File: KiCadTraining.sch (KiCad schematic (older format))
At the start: 57 parts

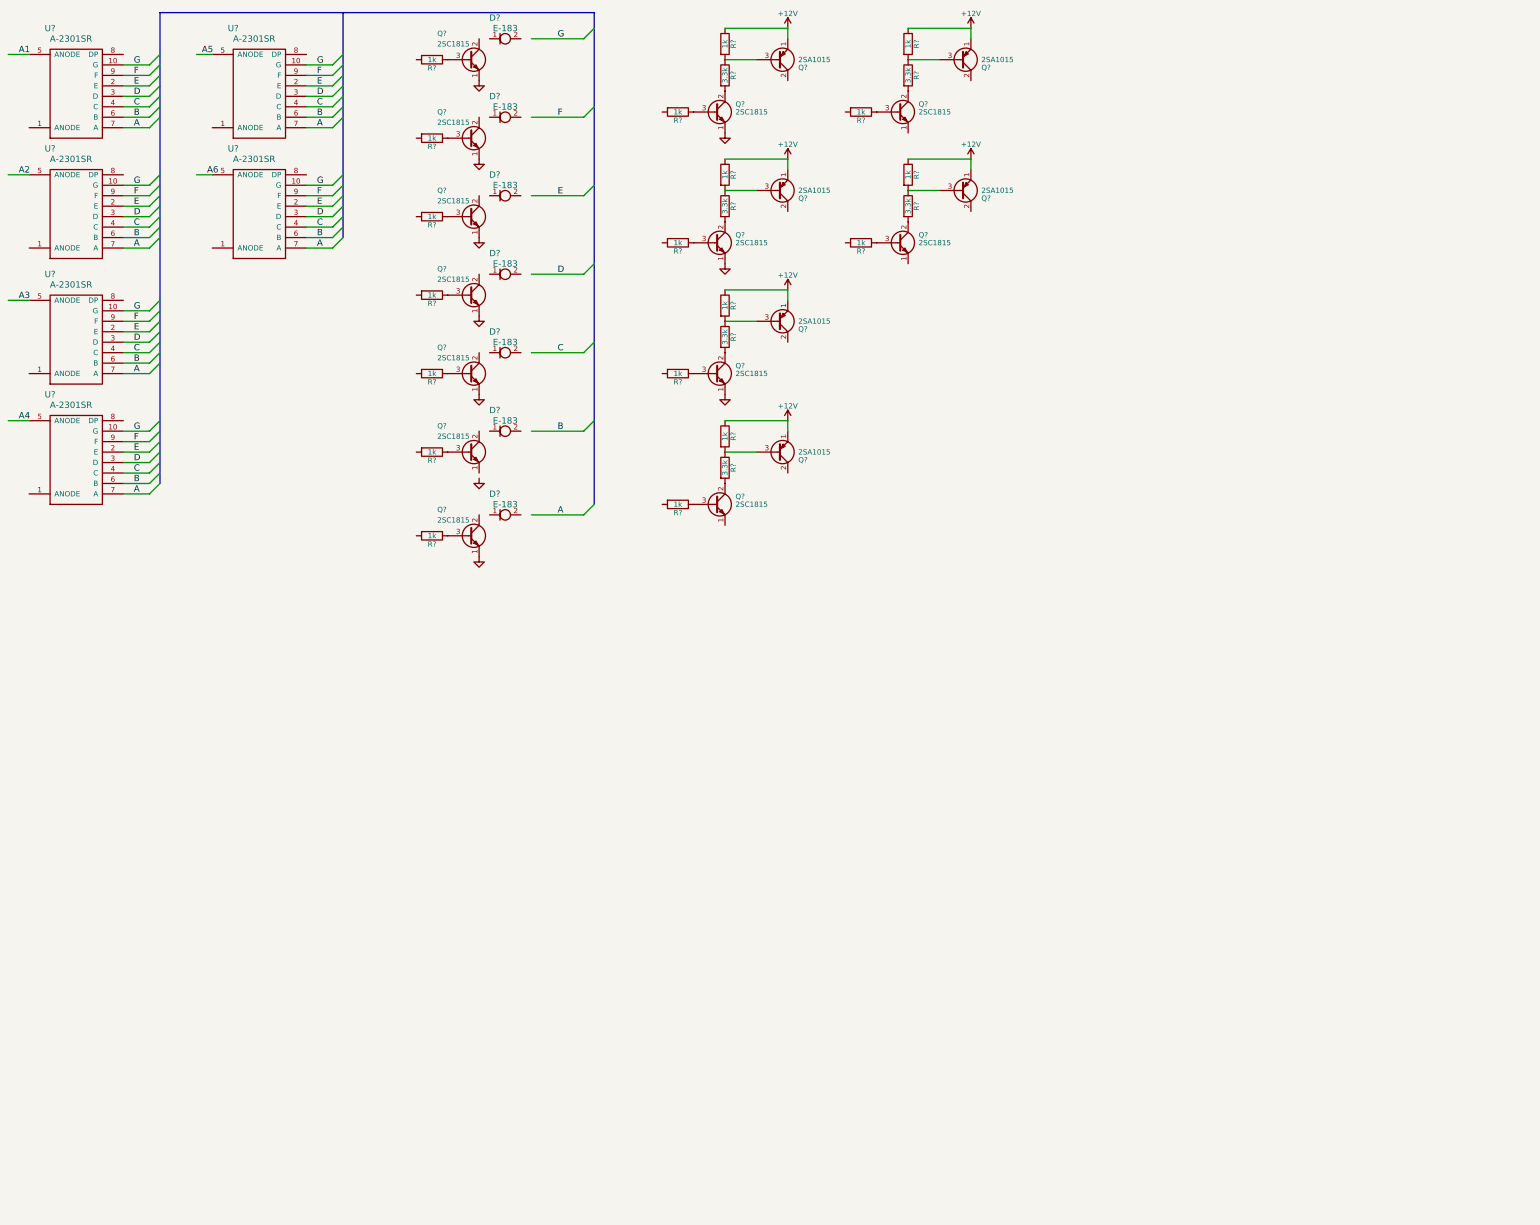
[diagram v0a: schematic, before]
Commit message: 7seg配線完了 STM32追加
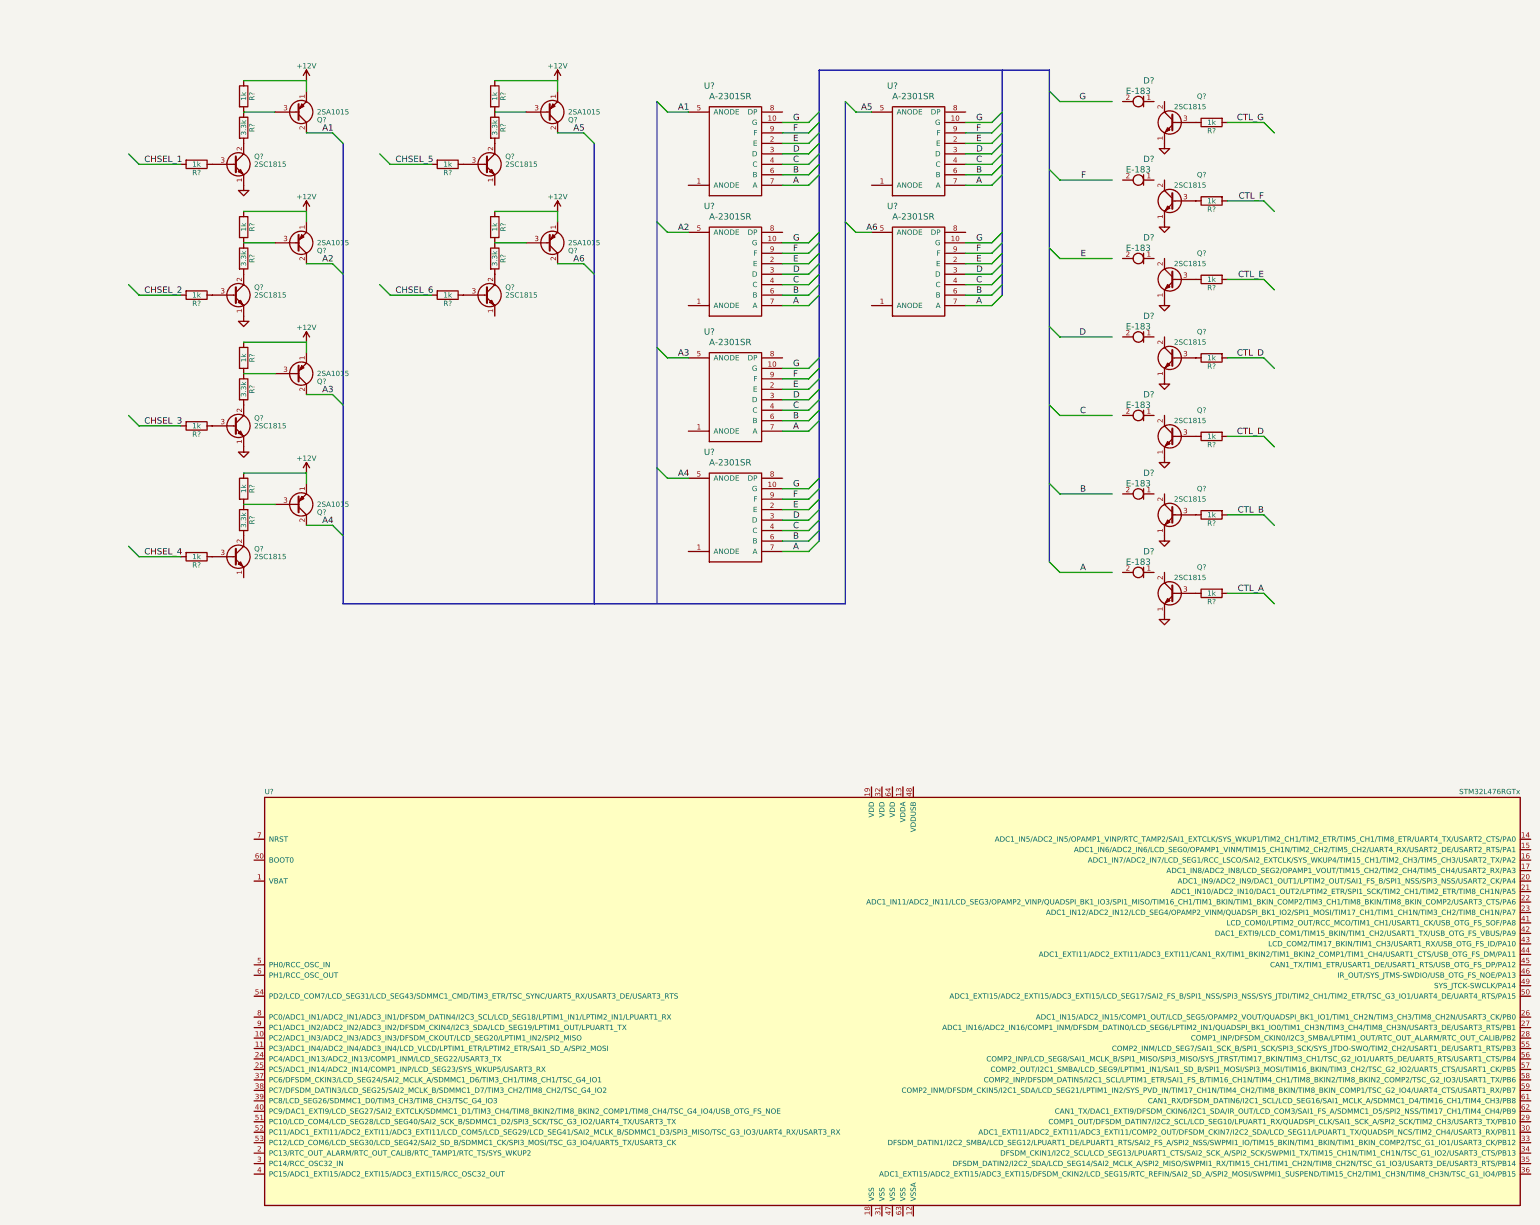
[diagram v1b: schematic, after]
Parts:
- added U?: STM32L476RGTx, LQFP64, symbol STM32L476RGTx
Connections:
- net labels added: CHSEL_1, CHSEL_2, CHSEL_3, CHSEL_4, CHSEL_5, CHSEL_6, CTL_A, CTL_B, CTL_D, CTL_E, CTL_F, CTL_G
- wire segments 73 -> 92
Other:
- moved on the sheet: D?, Q?, R?, U?

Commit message: Nucleo基板に修正 プッシュスイッチ 追加 RGB追加
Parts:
- removed U?: STM32L476RGTx, LQFP64, symbol STM32L476RGTx
- added D? (x2): LED_RABG, symbol LED_RABG
- added D? (x6): E-183, symbol E-183
- added Q? (x6): 2SC1815, TO_SOT_Packages_THT:TO-92_Molded_Narrow, symbol 2SC1815
- added R? (x6): R, symbol R
- added SW? (x5): SW_Push_Dual, symbol SW_Push_Dual
- added U?: STM32NUCLEO-L476RG, symbol STM32NUCLEO-L476RG
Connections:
- net labels added: BLUE_1, BLUE_2, CTL_C, GREEN_1, GREEN_2, POINT_CTL_1, POINT_CTL_2, POINT_SWP, RCVR_SEL, RED_1, RED_2, SVR_SEL
- wire segments 92 -> 140

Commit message: パッシブ部品の足を全てパッシブに変更
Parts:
- R26, R27, R28: renamed from R?; value R -> 1k
- gave numbers to parts that had none: 80
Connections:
- wire segments 140 -> 142
- no-connect marks 0 -> 72
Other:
- moved on the sheet: D1, D10, D11, D12, D13, D14, D15, D2, D3, D4, D5, D6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

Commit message: 部品レイアウト完了
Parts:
- D1, D10, D11, D12, D13, D14, D15, D2, D3, D4, D5, D6, D7: footprint (none) -> Diodes_THT:D_T-1_P10.16mm_Horizontal
- D8, D9: footprint (none) -> LEDs:LED_D5.0mm-4
- Q1, Q10, Q11, Q12, Q13, Q14, Q15, Q16, Q17, Q18, Q19, Q2, Q20, Q21, Q22, Q23, Q24, Q25, Q3, Q4, Q5, Q6, Q7, Q8, Q9: footprint TO_SOT_Packages_THT:TO-92_Molded_Narrow -> TO_SOT_Packages_THT:TO-92_Inline_Wide
- R1, R10, R11, R12, R13, R14, R15, R16, R17, R18, R19, R2, R20, R21, R22, R23, R24, R25, R26, R27, R28, R3, R4, R5, R6, R7, R8, R9: footprint (none) -> Resistors_THT:R_Axial_DIN0309_L9.0mm_D3.2mm_P12.70mm_Horizontal
- R29, R30, R31: value R -> 1k; footprint (none) -> Resistors_THT:R_Axial_DIN0309_L9.0mm_D3.2mm_P12.70mm_Horizontal
- SW1, SW2, SW3, SW4, SW5: footprint (none) -> Buttons_Switches_THT:SW_TH_Tactile_Omron_B3F-10xx
- U1: footprint (none) -> mylibSTM32Board:STM32L476NUCLEO
- U2, U3, U4, U5, U6, U7: footprint (none) -> mylib_segmentLED:A-2301SR
